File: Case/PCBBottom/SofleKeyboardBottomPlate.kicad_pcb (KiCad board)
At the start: 2 copper layers, 137.2 x 109.2 mm, 5 parts

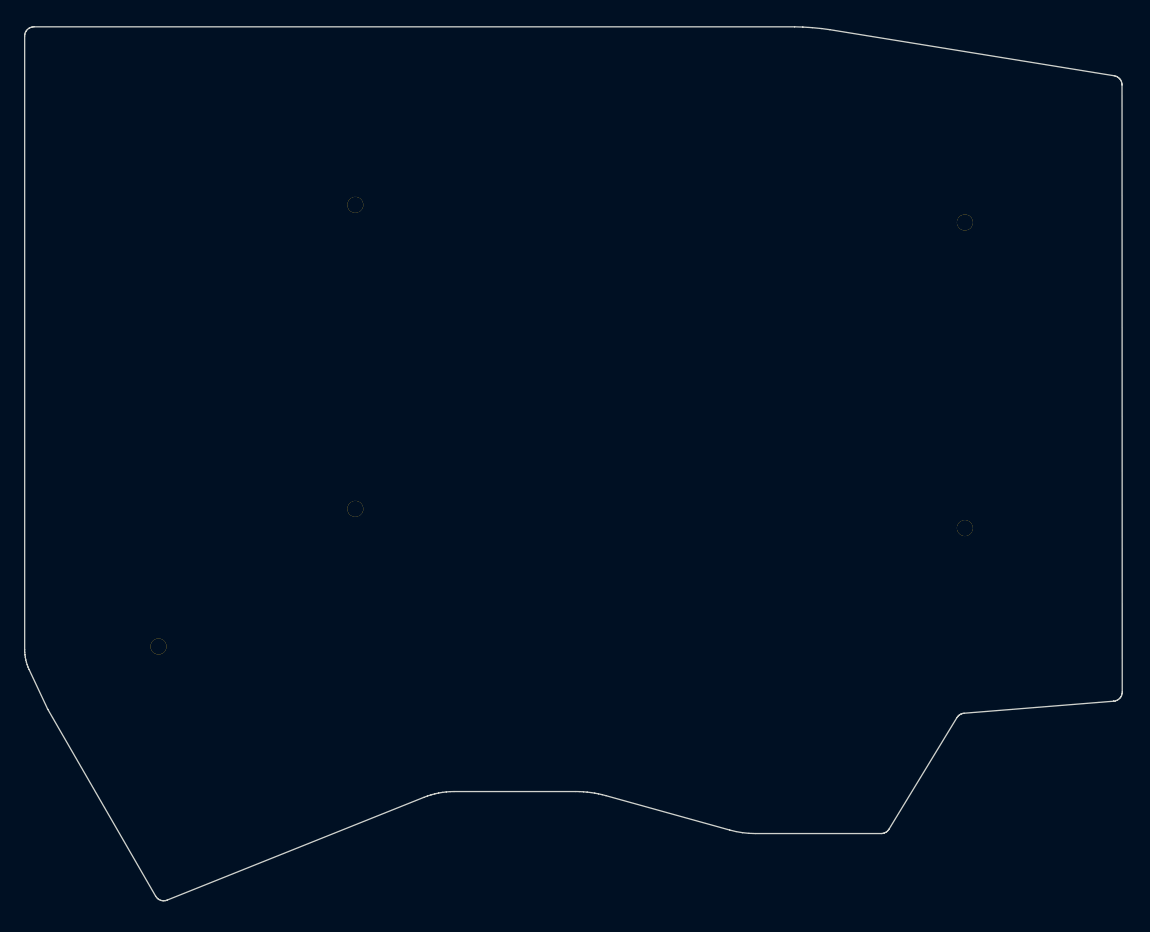
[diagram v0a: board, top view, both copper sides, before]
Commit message: Small changes to the bottom and top plates
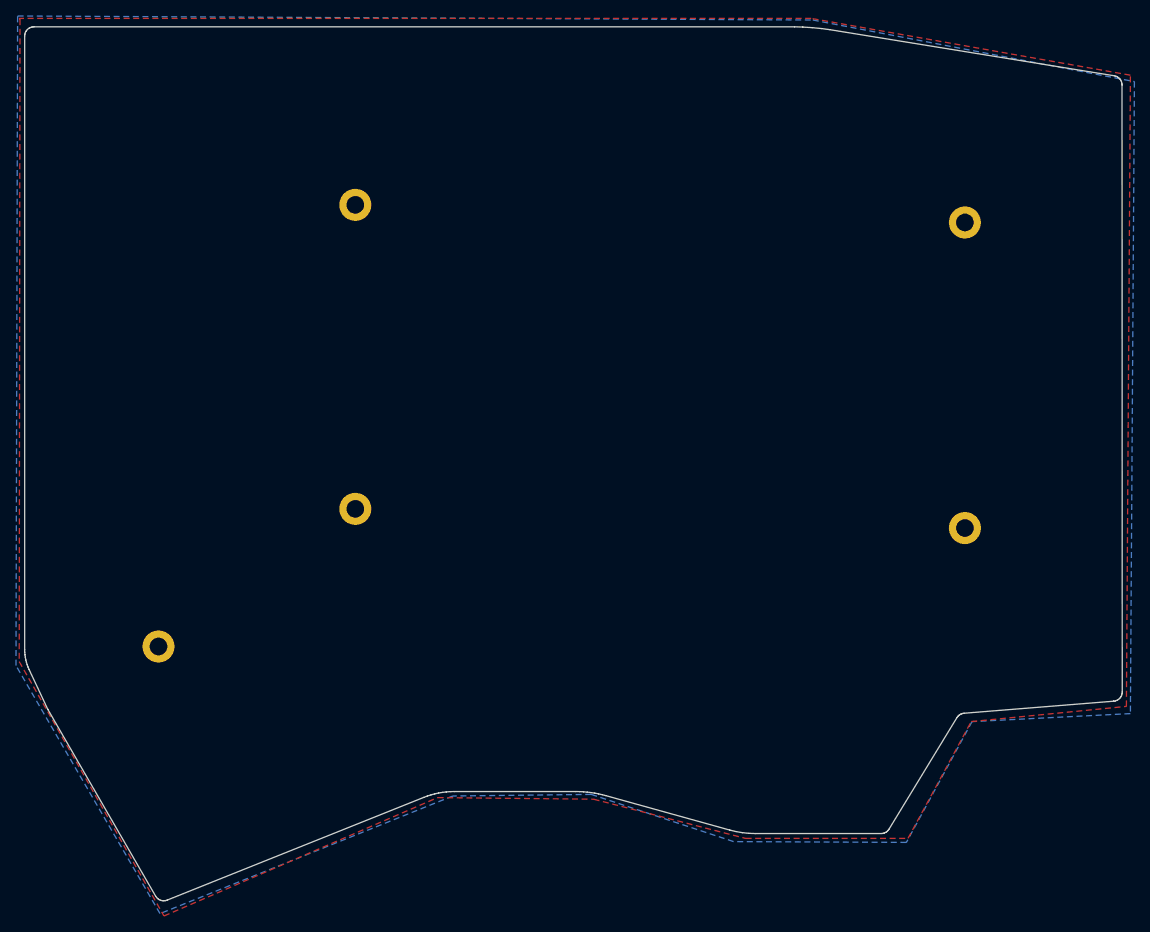
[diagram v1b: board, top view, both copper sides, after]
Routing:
- added copper zone on B.Cu, net (none)
- added copper zone on F.Cu, net (none)
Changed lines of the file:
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@@
   (layers
     (0 F.Cu signal)
-    (31 B.Cu signal)
-    (32 B.Adhes user)
-    (33 F.Adhes user)
-    (34 B.Paste user)
-    (35 F.Paste user)
-    (36 B.SilkS user)
-    (37 F.SilkS user)
-    (38 B.Mask user)
-    (39 F.Mask user)
-    (40 Dwgs.User user)
-    (41 Cmts.User user)
-    (42 Eco1.User user)
+    (31 B.Cu signal hide)
+    (32 B.Adhes user hide)
+    (33 F.Adhes user hide)
+    (34 B.Paste user hide)
+    (35 F.Paste user hide)
+    (36 B.SilkS user hide)
+    (37 F.SilkS user hide)
+    (38 B.Mask user hide)
+    (39 F.Mask user hide)
+    (40 Dwgs.User user hide)
+    (41 Cmts.User user hide)
+    (42 Eco1.User user hide)
     (43 Eco2.User user)
     (44 Edge.Cuts user)
-    (45 Margin user)
-    (46 B.CrtYd user)
-    (47 F.CrtYd user)
-    (48 B.Fab user)
-    (49 F.Fab user)
+    (45 Margin user hide)
+    (46 B.CrtYd user hide)
+    (47 F.CrtYd user hide)
+    (48 B.Fab user hide)
+    (49 F.Fab user hide)
   )
   (setup
@@
     (mod_text_size 1 1)
     (mod_text_width 0.15)
-    (pad_size 1.524 1.524)
-    (pad_drill 0.762)
+    (pad_size 4 4)
+    (pad_drill 2.2)
     (pad_to_mask_clearance 0.2)
     (aux_axis_origin 0 0)
@@
       (effects (font (size 1.27 1.27) (thickness 0.15)))
     )
-    (pad 1 thru_hole circle (at 0 0) (size 2 2) (drill 2) (layers *.Cu *.Mask))
+    (pad 1 thru_hole circle (at 0 0) (size 4 4) (drill 2.2) (layers *.Cu *.Mask Dwgs.User))
   )
   (module Wire_Pads:SolderWirePad_single_0-8mmDrill (layer F.Cu)
@@
       (effects (font (size 1.27 1.27) (thickness 0.15)))
     )
-    (pad 2 thru_hole circle (at 0 0) (size 2 2) (drill 2) (layers *.Cu *.Mask))
+    (pad 2 thru_hole circle (at 0 0) (size 4 4) (drill 2.2) (layers *.Cu *.Mask Dwgs.User))
   )
   (module Wire_Pads:SolderWirePad_single_0-8mmDrill (layer F.Cu)
@@
       (effects (font (size 1.27 1.27) (thickness 0.15)))
     )
-    (pad 3 thru_hole circle (at 0 0) (size 2 2) (drill 2) (layers *.Cu *.Mask))
+    (pad 3 thru_hole circle (at 0 0) (size 4 4) (drill 2.2) (layers *.Cu *.Mask Dwgs.User))
   )
   (module Wire_Pads:SolderWirePad_single_0-8mmDrill (layer F.Cu)
@@
       (effects (font (size 1.27 1.27) (thickness 0.15)))
     )
-    (pad 4 thru_hole circle (at 0 0) (size 2 2) (drill 2) (layers *.Cu *.Mask))
+    (pad 4 thru_hole circle (at 0 0) (size 4 4) (drill 2.2) (layers *.Cu *.Mask Dwgs.User))
   )
   (module Wire_Pads:SolderWirePad_single_0-8mmDrill (layer F.Cu)
@@
       (effects (font (size 1.27 1.27) (thickness 0.15)))
     )
-    (pad 5 thru_hole circle (at 0 0) (size 2 2) (drill 2) (layers *.Cu *.Mask))
+    (pad 5 thru_hole circle (at 0 0) (size 4 4) (drill 2.2) (layers *.Cu *.Mask Dwgs.User))
   )
   (gr_line (start 156.72 103.850003) (end 138.00693 105.35553) (layer Edge.Cuts) (width 0.1))
@@
   (gr_line (start 156.71997 103.850003) (end 156.72 103.850003) (layer Edge.Cuts) (width 0.1))
   (gr_line (start 156.72 103.850003) (end 156.72 103.850003) (layer Edge.Cuts) (width 0.1))
+  (zone (net 0) (net_name "") (layer F.Cu) (hatch edge 0.508)
+    (connect_pads (clearance 0.508))
+    (min_thickness 0.254)
+    (fill yes (arc_segments 32) (thermal_gap 0.508) (thermal_bridge_width 0.508))
+    (polygon
+      (pts
+        (xy 20 18.6) (xy 19.9 98.9) (xy 38 130.7) (xy 72.2 115.9) (xy 91.7 116.1)
+        (xy 110.7 121) (xy 131 121) (xy 138.9 106.4) (xy 158.3 104.5) (xy 158.8 25.6)
+        (xy 118.9 18.5) (xy 19.9 18.5)
+      )
+    )
+  )
+  (zone (net 0) (net_name "") (layer B.Cu) (hatch edge 0.508)
+    (connect_pads (clearance 0.508))
+    (min_thickness 0.254)
+    (fill yes (arc_segments 32) (thermal_gap 0.508) (thermal_bridge_width 0.508))
+    (polygon
+      (pts
+        (xy 19.7 18.2) (xy 119.1 18.7) (xy 159.3 26.4) (xy 158.8 105.4) (xy 139 106.4)
+        (xy 130.8 121.5) (xy 109.2 121.4) (xy 91.4 115.5) (xy 74.1 115.7) (xy 37.5 130.4)
+        (xy 19.5 99.4)
+      )
+    )
+  )
 )

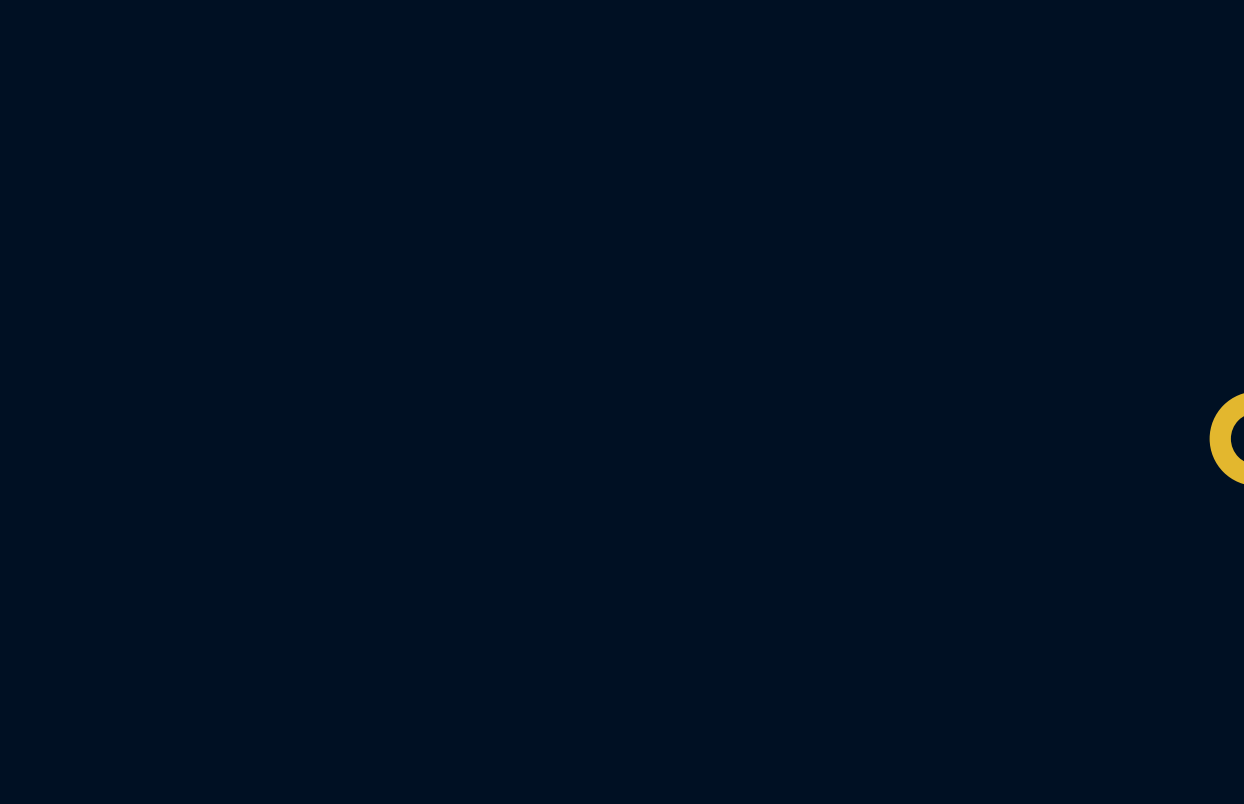
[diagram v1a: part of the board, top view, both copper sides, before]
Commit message: Add first version of logo
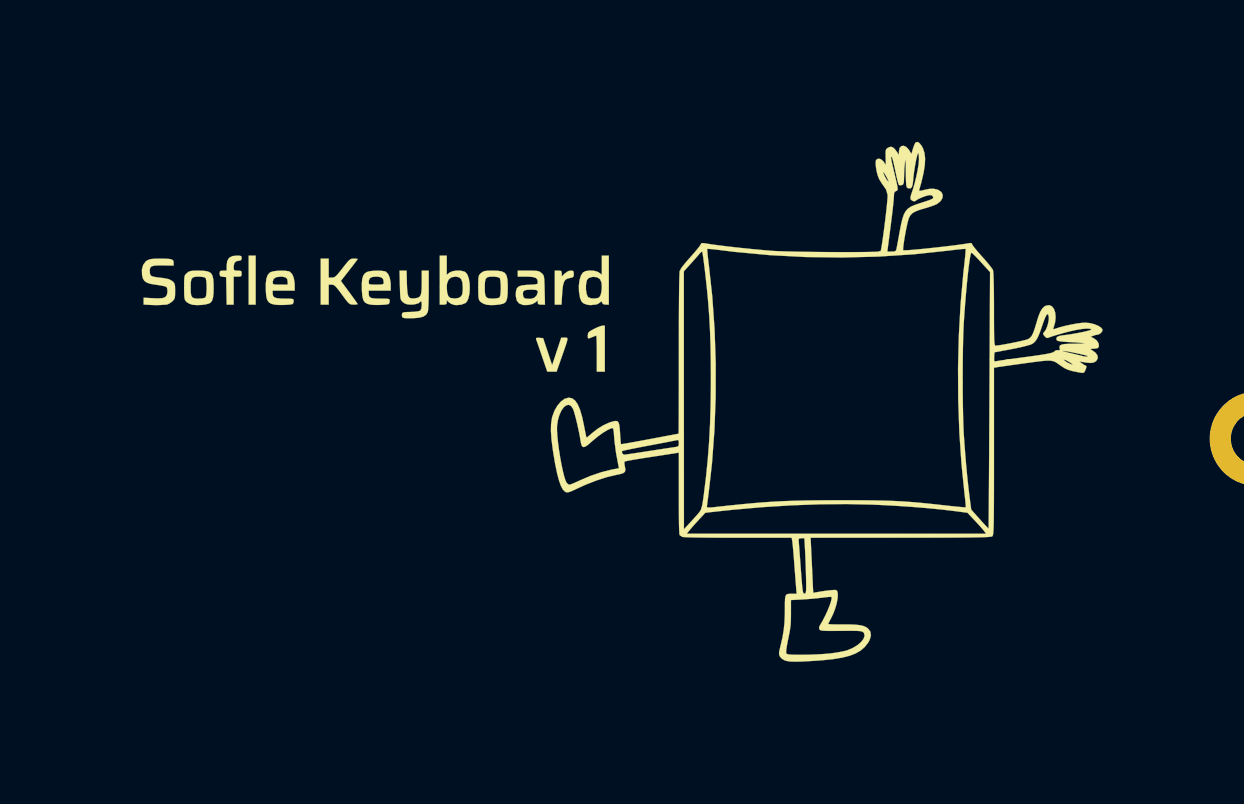
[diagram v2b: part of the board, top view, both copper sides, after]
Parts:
- added Ref**: Val**, SofleKeyboardBottomPlate:logo1, B.Cu at (102.5, 45.9)
- added Ref**: Val**, SofleKeyboardBottomPlate:logo1, F.Cu at (118.3, 46.2)

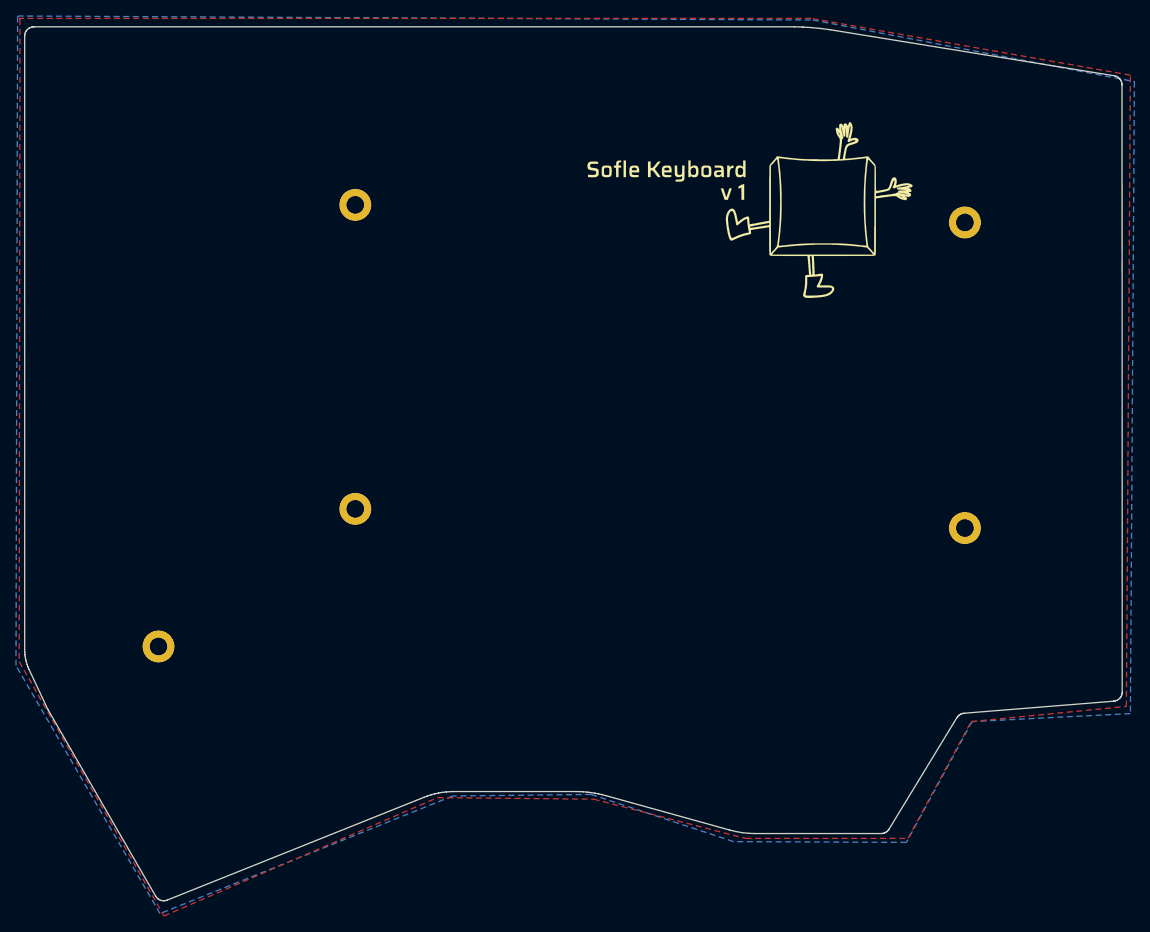
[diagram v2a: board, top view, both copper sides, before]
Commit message: Finish logo, add the logo and credits on the bottom plate
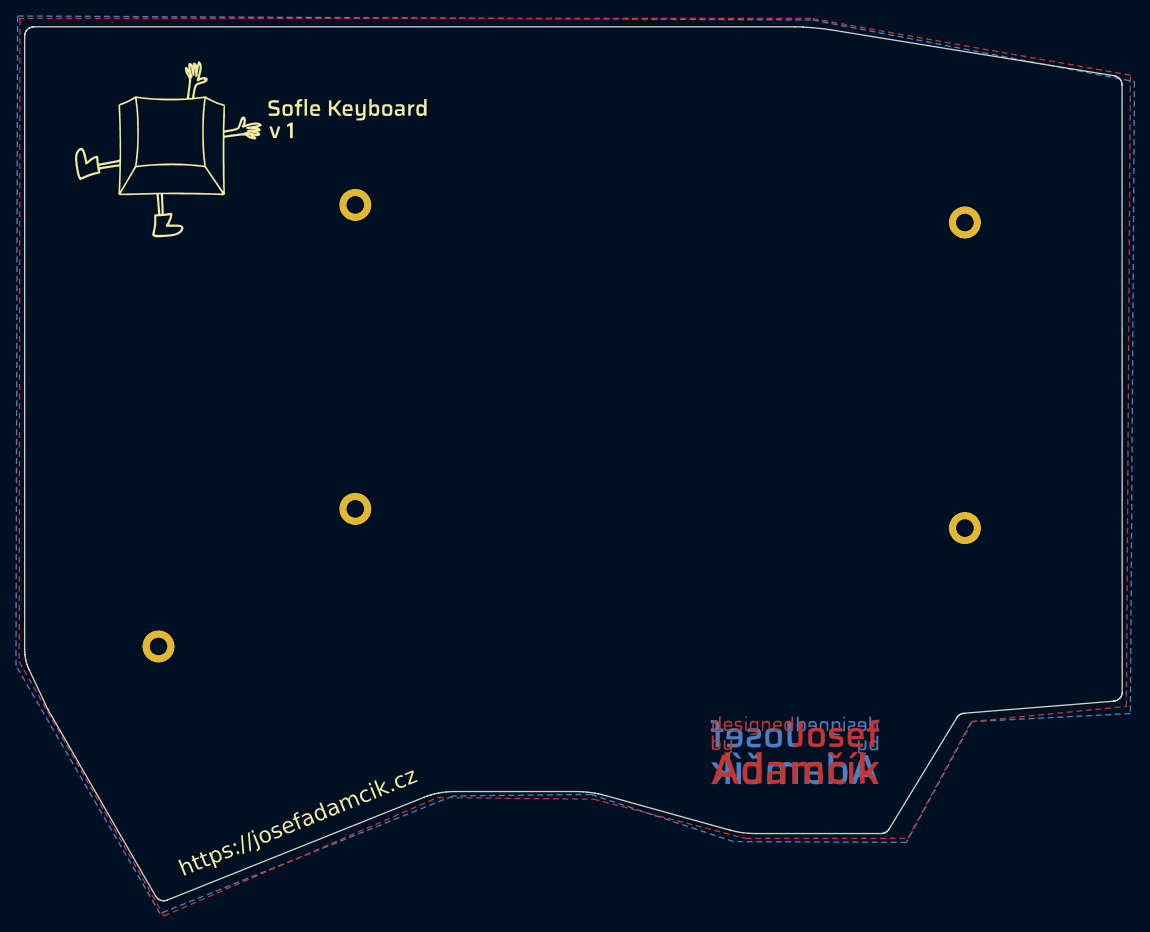
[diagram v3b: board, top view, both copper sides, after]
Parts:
- removed the Ref** at (102.5, 45.9)
- removed the Ref** at (118.3, 46.2)
- added Ref**: Val**, logos:josef_adamcik_20mm_cu_mask, B.Cu at (117.2, 114.0)
- added Ref**: Val**, logos:josef_adamcik_20mm_cu_mask, F.Cu at (116.6, 113.9)
- added Ref**: Val**, SofleKeyboardBottomPlate:SofleLogo2, F.Cu at (37.0, 38.6)
- added Ref**: Val**, SofleKeyboardBottomPlate:SofleLogo1, B.Cu at (40.6, 39.0)
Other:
- board text added: "https://josefadamcik.cz"
